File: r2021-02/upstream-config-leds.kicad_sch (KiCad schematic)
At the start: 59 parts, among them J5 Conn_01x03_Male, J8 USB_A male UP, J9 USB_B_Micro (up), U1 2k i2c eeprom, U12 NUP4202, U3 USB2517, Y1 24MHz

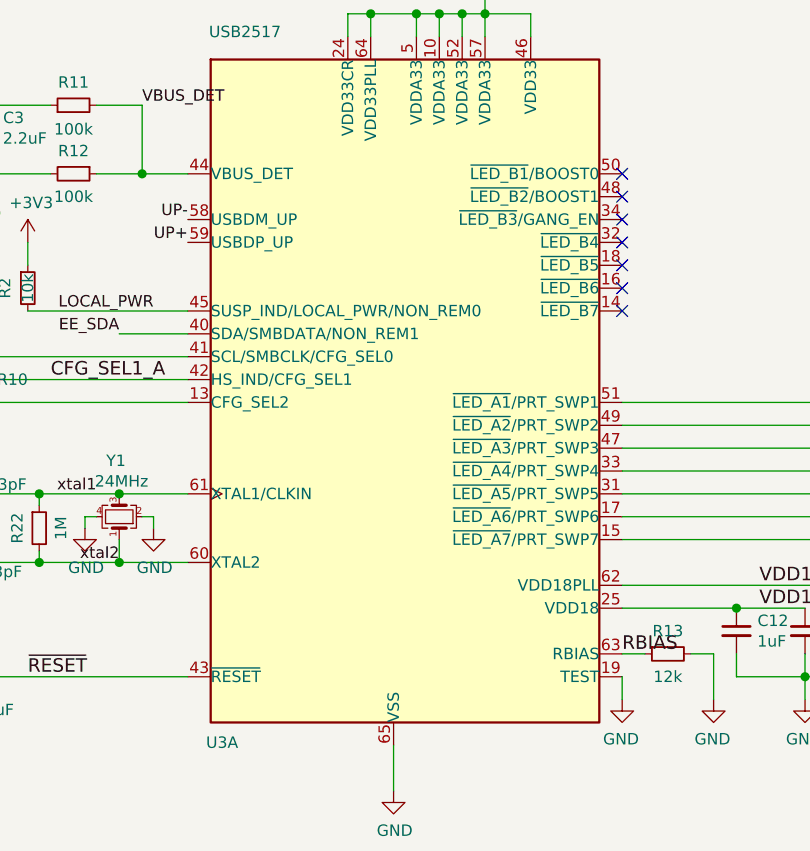
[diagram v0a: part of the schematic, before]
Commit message: restore to kicad 6.0 compatibility
updated to my footprintbranch, 6.0 and all that
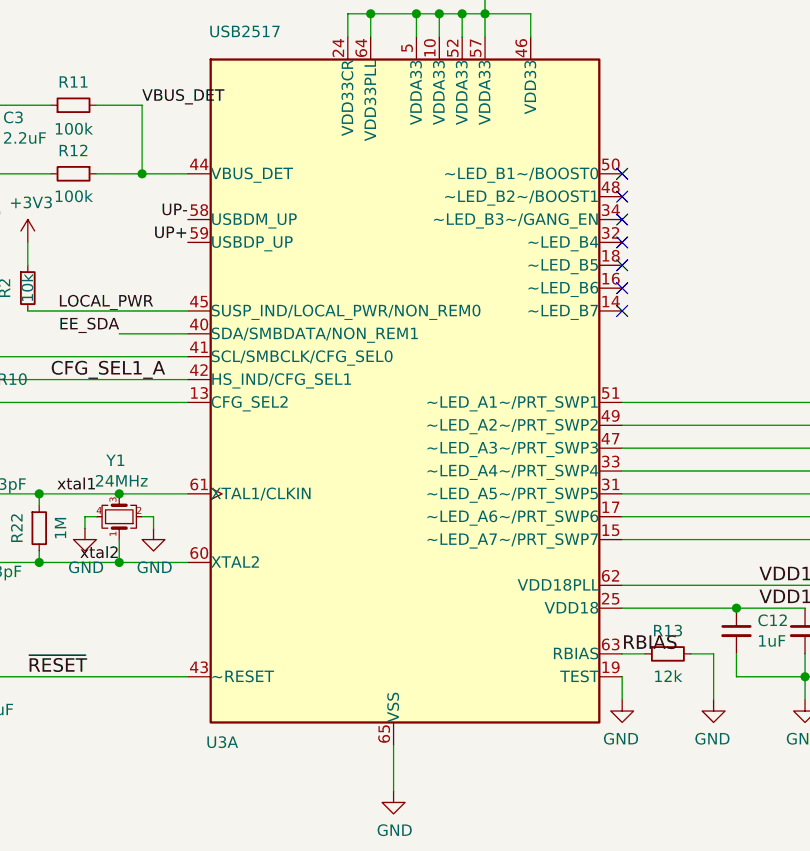
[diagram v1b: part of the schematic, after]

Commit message: overhaul, push silk, complete "again"
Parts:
- renumbered C35 to C1, C9 to C10, C10 to C11, C11 to C12, C12 to C13, C13 to C14, C14 to C15, C15 to C16, C16 to C17, C17 to C18, C18 to C19, C32 to C2, C2 to C3, C5 to C4, C4 to C5, C3 to C6, C6 to C7, C7 to C8, C8 to C9, D3 to D1, D11 to D10, D9 to D3, D10 to D9, J5 to J1, J8 to J2, J9 to J3, R21 to R1, R2 to R11, R22 to R12, R11 to R13, R12 to R14, R13 to R15, R14 to R16, R15 to R17, R16 to R18, R17 to R19, R1 to R2, R18 to R20, R19 to R21, R20 to R22, U12 to U2
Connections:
- net LED_A6: now also R22.1; no longer R21.1
- net LED_A7: now also R21.1; no longer R22.1
- net LA_6-6 renamed LA_7-6
- net LA_7-5 renamed LA_6-5
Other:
- moved on the sheet: R21, R22

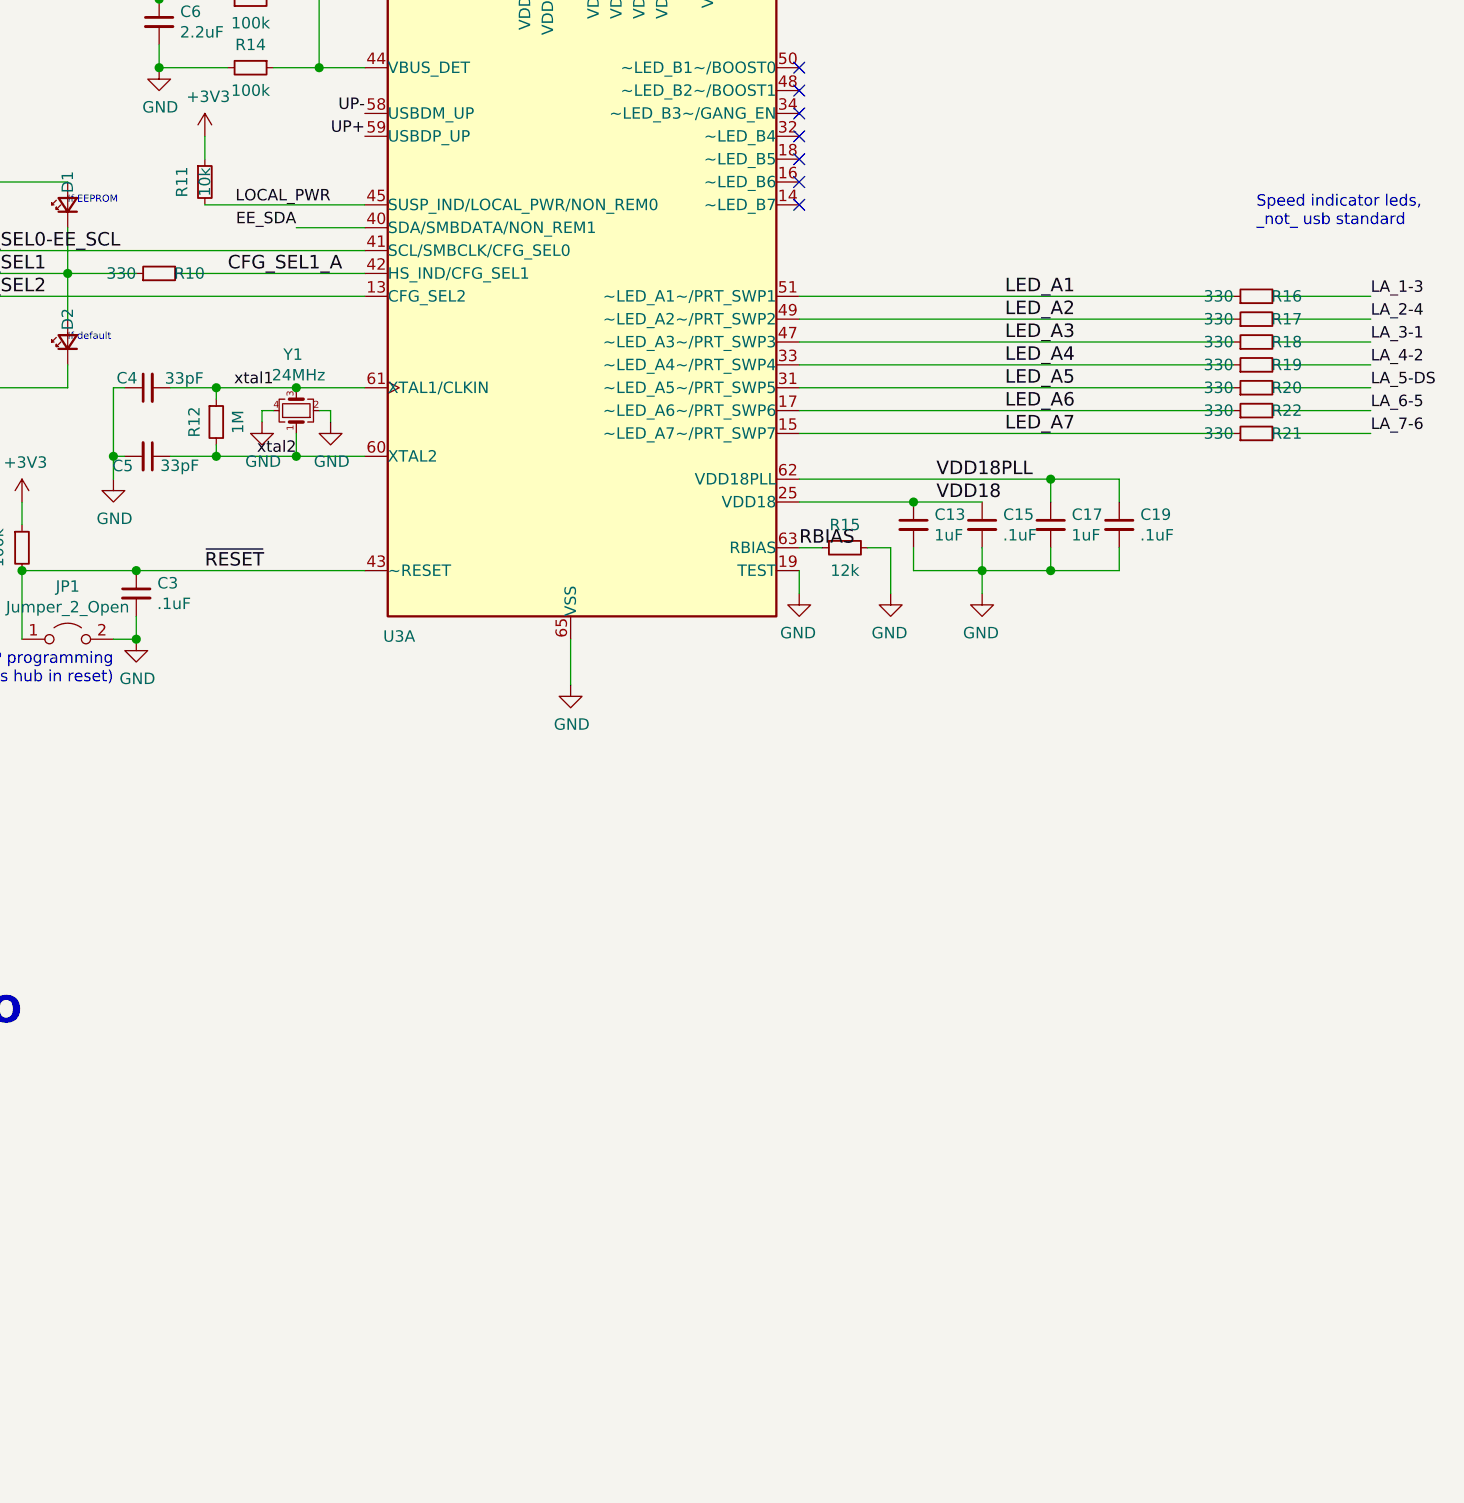
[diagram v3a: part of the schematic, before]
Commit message: r2: push more, switch to m3 mounting, more silk
added a chicken jumper to connect vbus and 5v...
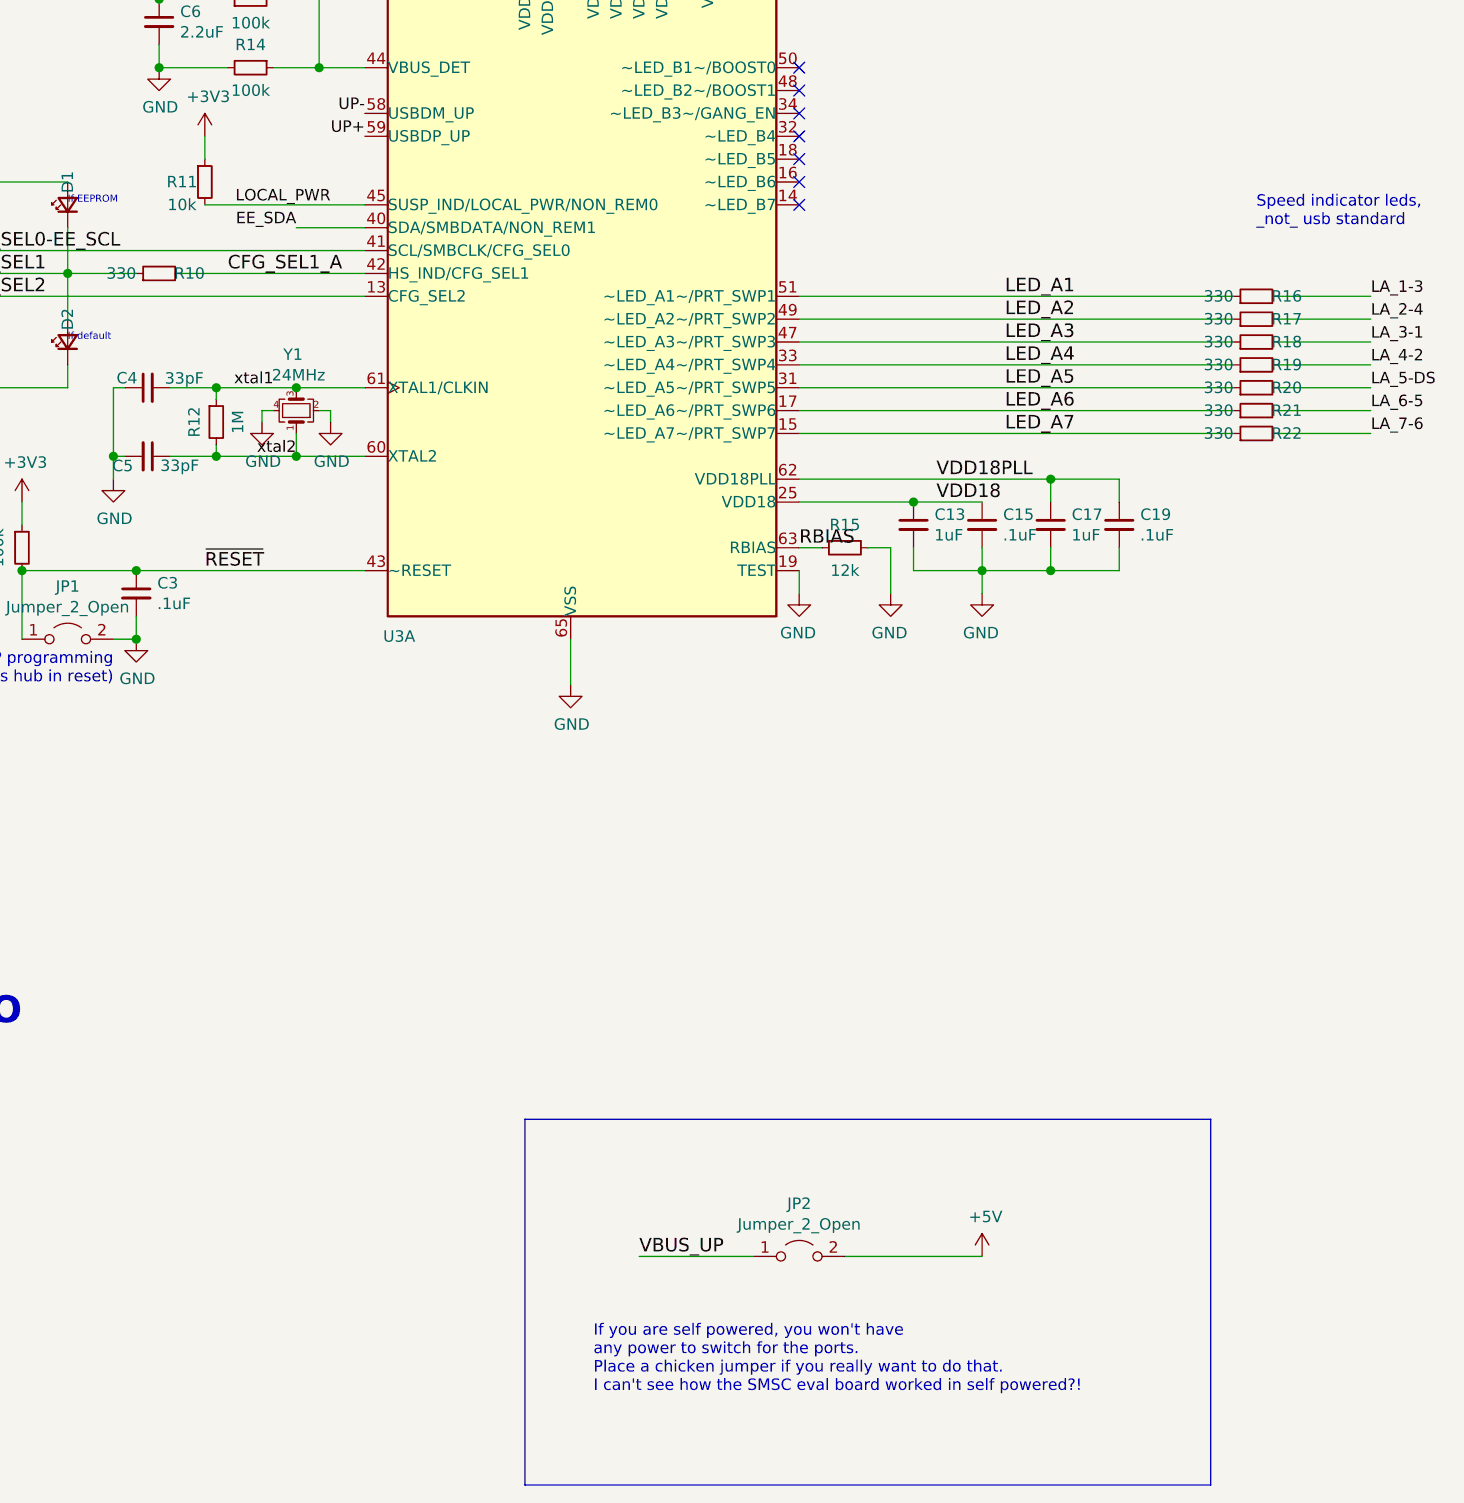
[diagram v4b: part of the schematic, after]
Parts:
- added JP2: Jumper_2_Open, TestPoint:TestPoint_2Pads_Pitch2.54mm_Drill0.8mm, symbol Jumper:Jumper_2_Open
- renumbered R22 to R21, R21 to R22
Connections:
- net VBUS_UP: now also JP2.1 (A)
- new net +5V: JP2.2 (B)
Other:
- note added: "If you are self powered, you won't have any power to switch for the ports. Place a chicken jumper if you really want to do that. I can't see how the SMSC eval board worked in self powered?!"
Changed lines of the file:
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@@
     (stroke (width 0) (type solid) (color 0 0 0 0))
+  )
+  (wire (pts (xy 215.9 203.2) (xy 228.6 203.2))
+    (stroke (width 0) (type default) (color 0 0 0 0))
   )
   (wire (pts (xy 248.92 38.1) (xy 248.92 40.64))
@@
     (stroke (width 0) (type solid) (color 0 0 0 0))
   )
+  (polyline (pts (xy 203.2 187.96) (xy 279.4 187.96))
+    (stroke (width 0) (type default) (color 0 0 0 0))
+  )
   (wire (pts (xy 208.28 134.62) (xy 208.28 139.7))
     (stroke (width 0) (type solid) (color 0 0 0 0))
@@
     (stroke (width 0) (type solid) (color 0 0 0 0))
   )
+  (polyline (pts (xy 279.4 187.96) (xy 279.4 228.6))
+    (stroke (width 0) (type default) (color 0 0 0 0))
+  )
   (wire (pts (xy 83.82 162.56) (xy 73.66 162.56))
     (stroke (width 0) (type solid) (color 0 0 0 0))
@@
     (stroke (width 0) (type solid) (color 0 0 0 0))
   )
+  (wire (pts (xy 238.76 203.2) (xy 254 203.2))
+    (stroke (width 0) (type default) (color 0 0 0 0))
+  )
   (wire (pts (xy 132.08 99.06) (xy 132.08 96.52))
     (stroke (width 0) (type solid) (color 0 0 0 0))
@@
     (stroke (width 0) (type solid) (color 0 0 0 0))
   )
+  (polyline (pts (xy 279.4 228.6) (xy 203.2 228.6))
+    (stroke (width 0) (type default) (color 0 0 0 0))
+  )
   (wire (pts (xy 261.62 116.84) (xy 269.24 116.84))
     (stroke (width 0) (type solid) (color 0 0 0 0))
@@
   (wire (pts (xy 88.9 149.86) (xy 96.52 149.86))
     (stroke (width 0) (type solid) (color 0 0 0 0))
+  )
+  (polyline (pts (xy 203.2 228.6) (xy 203.2 187.96))
+    (stroke (width 0) (type default) (color 0 0 0 0))
   )
   (wire (pts (xy 350.52 149.86) (xy 350.52 167.64))
@@
     (effects (font (size 1.27 1.27)) (justify left bottom))
   )
+  (text "If you are self powered, you won't have\nany power to switch for the ports.\nPlace a chicken jumper if you really want to do that.\nI can't see how the SMSC eval board worked in self powered?!"
+    (at 210.82 218.44 0)
+    (effects (font (size 1.27 1.27)) (justify left bottom))
+  )
   (text "Near CDD33CR (24)" (at 208.28 27.94 180)
     (effects (font (size 0.9906 0.9906)) (justify right bottom))
@@
   )
   (label "CFG_SEL1_A" (at 170.18 93.98 0) (fields_autoplaced)
+    (effects (font (size 1.4986 1.4986)) (justify left bottom))
+  )
+  (label "VBUS_UP" (at 215.9 203.2 0) (fields_autoplaced)
     (effects (font (size 1.4986 1.4986)) (justify left bottom))
   )
@@
   (symbol (lib_id "power:+3V3") (at 320.04 40.64 0) (unit 1)
     (in_bom yes) (on_board yes)
-    (property "Reference" "#PWR032" (id 0) (at 320.04 44.45 0)
+    (property "Reference" "#PWR033" (id 0) (at 320.04 44.45 0)
       (effects (font (size 1.27 1.27)) hide)
     )
@@
   (symbol (lib_id "Device:R_Small") (at 284.48 111.76 90) (unit 1)
     (in_bom yes) (on_board yes)
-    (property "Reference" "R21" (id 0) (at 289.56 111.76 90)
+    (property "Reference" "R22" (id 0) (at 289.56 111.76 90)
       (effects (font (size 1.27 1.27)) (justify left))
     )
@@
   (symbol (lib_id "Device:R_Small") (at 284.48 109.22 90) (unit 1)
     (in_bom yes) (on_board yes)
-    (property "Reference" "R22" (id 0) (at 289.56 109.22 90)
+    (property "Reference" "R21" (id 0) (at 289.56 109.22 90)
       (effects (font (size 1.27 1.27)) (justify left))
     )
@@
   (symbol (lib_id "power:GND") (at 350.52 170.18 0) (unit 1)
     (in_bom yes) (on_board yes)
-    (property "Reference" "#PWR033" (id 0) (at 350.52 176.53 0)
+    (property "Reference" "#PWR034" (id 0) (at 350.52 176.53 0)
       (effects (font (size 1.27 1.27)) hide)
     )
@@
   (symbol (lib_id "Device:R_Small") (at 167.64 83.82 0) (unit 1)
     (in_bom yes) (on_board yes)
-    (property "Reference" "R11" (id 0) (at 165.1 83.82 90))
-    (property "Value" "10k" (id 1) (at 167.64 83.82 90))
+    (property "Reference" "R11" (id 0) (at 165.1 83.82 0))
+    (property "Value" "10k" (id 1) (at 165.1 86.36 0))
     (property "Footprint" "Resistor_SMD:R_0603_1608Metric" (id 2) (at 167.64 83.82 0)
       (effects (font (size 1.27 1.27)) hide)
@@
     (pin "1")
   )
+  (symbol (lib_id "Jumper:Jumper_2_Open") (at 233.68 203.2 0) (unit 1)
+    (in_bom yes) (on_board yes)
+    (property "Reference" "JP2" (id 0) (at 233.68 197.3388 0))
+    (property "Value" "Jumper_2_Open" (id 1) (at 233.68 199.6375 0))
+    (property "Footprint" "TestPoint:TestPoint_2Pads_Pitch2.54mm_Drill0.8mm" (id 2) (at 233.68 203.2 0)
+      (effects (font (size 1.27 1.27)) hide)
+    )
+    (property "Datasheet" "~" (id 3) (at 233.68 203.2 0)
+      (effects (font (size 1.27 1.27)) hide)
+    )
+    (pin "1")
+    (pin "2")
+  )
   (symbol (lib_id "power:GNDPWR") (at 48.26 48.26 0) (unit 1)
     (in_bom yes) (on_board yes)
@@
     (pin "2")
   )
+  (symbol (lib_id "power:+5V") (at 254 203.2 0) (unit 1)
+    (in_bom yes) (on_board yes)
+    (property "Reference" "#PWR032" (id 0) (at 254 207.01 0)
+      (effects (font (size 1.27 1.27)) hide)
+    )
+    (property "Value" "+5V" (id 1) (at 254.381 198.8058 0))
+    (property "Footprint" "" (id 2) (at 254 203.2 0)
+      (effects (font (size 1.27 1.27)) hide)
+    )
+    (property "Datasheet" "" (id 3) (at 254 203.2 0)
+      (effects (font (size 1.27 1.27)) hide)
+    )
+    (pin "1")
+  )
   (symbol (lib_id "Device:R_Small") (at 168.91 110.49 0) (unit 1)
